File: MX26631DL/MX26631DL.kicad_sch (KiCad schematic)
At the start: 14 parts, among them U1 ESDBW5V0A1_C5173252, U2 MX26631DL

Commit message: Testboard is done, production files generated
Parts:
- removed C17: 100nF, Capacitor_SMD:C_0402_1005Metric, symbol Device:C
- removed U1: ESDBW5V0A1_C5173252, easyeda2kicad:X1-DFN1006-2_L1.0-W0.6-P0.65-BI, symbol TVS diode:ESDBW5V0A1_C5173252
- added U4: TPESD0402G15V, Diode_SMD:D_0402_1005Metric, symbol TVS diode:ESDBW5V0A1_C5173252
- C16: value 100nF -> 10uF; LCSC Part C1525 -> C315248
- R10: value 11kR -> 6.2kR; LCSC Part C2909313 -> C25915
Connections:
- net +5V_unprot: now also U4.1 (K)
- net GND: now also U4.2 (A)
- no-connect marks 11 -> 12
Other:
- note added: "For testing overvoltage and overcurrent capability. Overvoltage Threshold = 5.929v Overcurrent Threshold = 5.49A (8.235A in short bursts) Testing Over-voltage Protection V = 12V Testing Over-current Protection V = 5V - When testing overvoltage, a maximum of 12V to prevent LED burnout"
- note removed: "For testing overvoltage and overcurrent capability. Overvoltage = 6v Overcurrent = 3.26A(5A in short bursts) - When testing overvoltage, a maximum of 12V to prevent LED burnout"
- moved on the sheet: D1, R1

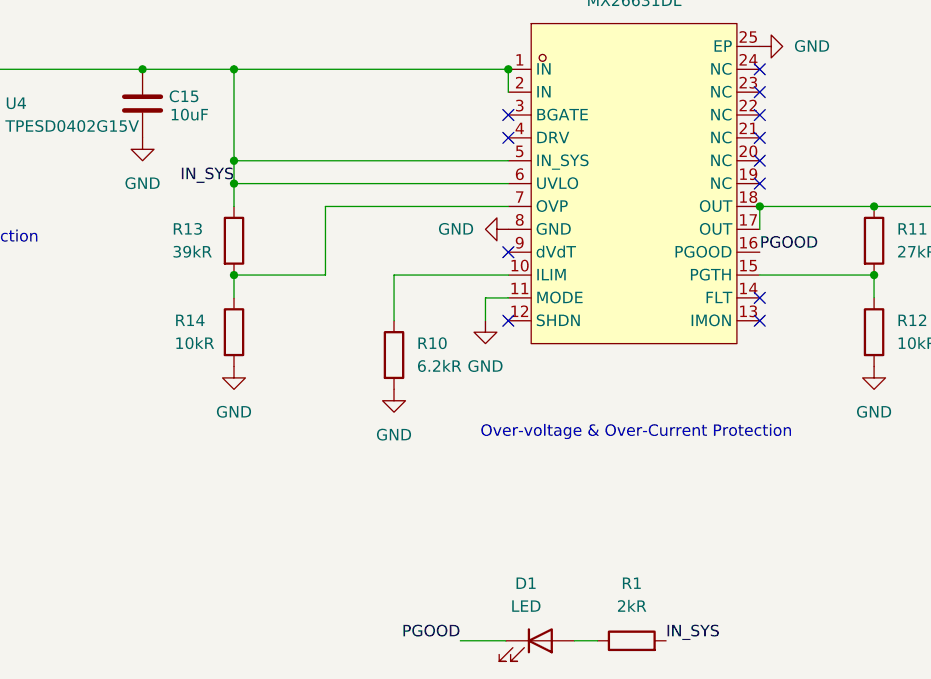
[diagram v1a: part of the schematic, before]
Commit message: Added dVdT capacitor to reduce current inrush. Production files generated
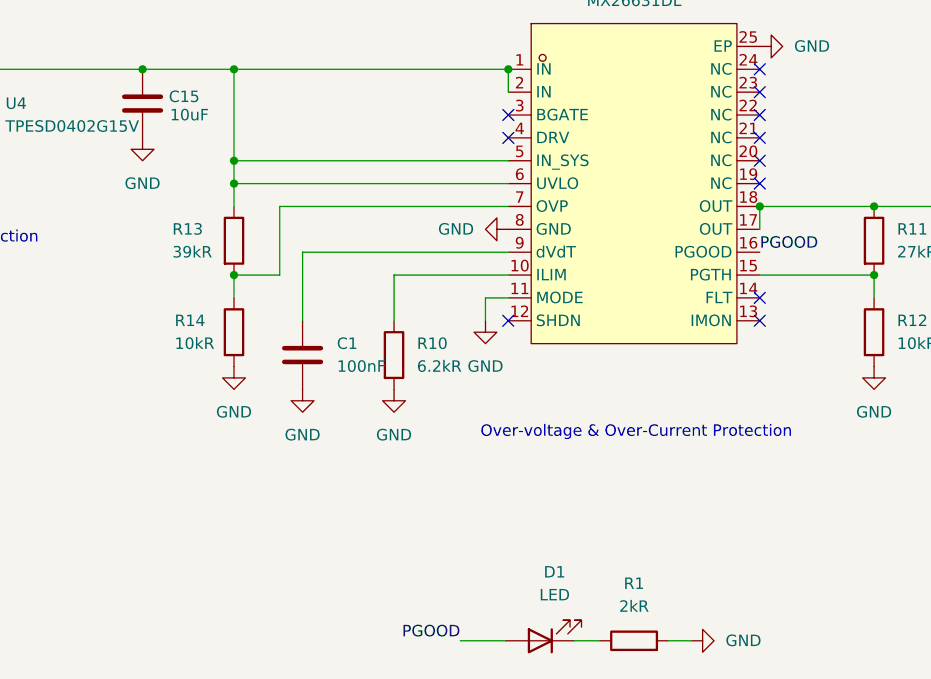
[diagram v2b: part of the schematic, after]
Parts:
- added C1: 100nF, Capacitor_SMD:C_0201_0603Metric, symbol Device:C
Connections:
- net +5V_unprot: no longer R1.2
- net GND: now also R1.2, C1.2
- net PGOOD: now also D1.2 (A); no longer D1.1 (K)
- net at R1.1: now also D1.1 (K); no longer D1.2 (A)
- net at U2.9 (dVdT): now also C1.1
- no-connect marks 12 -> 11
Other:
- moved on the sheet: D1

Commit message: Need to verify circuit 1 more time
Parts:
- removed C15, C16: 10uF, Capacitor_SMD:C_0402_1005Metric, symbol Device:C
- removed H1: X6511WV-02H-C30D60, easyeda2kicad:HDR-TH_2P-P2.54-V-M, symbol 2-pin header:X6511WV-02H-C30D60
- removed R2: 2R, Package_TO_SOT_SMD:TO-263-2, symbol Device:R
- added C2: 100nF, Capacitor_SMD:C_0402_1005Metric_Pad0.74x0.62mm_HandSolder, symbol Device:C
- added C3: 10uF, Capacitor_SMD:C_0805_2012Metric_Pad1.18x1.45mm_HandSolder, symbol Device:C
- added R7: 10R, Resistor_SMD:R_0603_1608Metric_Pad0.98x0.95mm_HandSolder, symbol Device:R
- added U1, U2: ZX-PZ2.54-1-1PZZ, easyeda2kicad:HDR-TH_1P-P2.54-V-M, symbol Pin header:ZX-PZ2.54-1-1PZZ
- C1: value 100nF -> 10uF; footprint Capacitor_SMD:C_0201_0603Metric -> Capacitor_SMD:C_0805_2012Metric_Pad1.18x1.45mm_HandSolder; LCSC Part C76939 -> C95841
- R1: renamed from R13; footprint Resistor_SMD:R_0402_1005Metric -> Resistor_SMD:R_0402_1005Metric_Pad0.72x0.64mm_HandSolder
- R2: renamed from R14; footprint Resistor_SMD:R_0402_1005Metric -> Resistor_SMD:R_0402_1005Metric_Pad0.72x0.64mm_HandSolder
- R3: renamed from R10; value 6.2kR -> 20kR; footprint Resistor_SMD:R_0402_1005Metric -> Resistor_SMD:R_0603_1608Metric_Pad0.98x0.95mm_HandSolder; LCSC Part C25915 -> C2907011
- R5: renamed from R11; value 27kR -> 31.6kR; footprint Resistor_SMD:R_0402_1005Metric -> Resistor_SMD:R_0603_1608Metric; LCSC Part C138022 -> C2933196
- R6: renamed from R12; footprint Resistor_SMD:R_0402_1005Metric -> Resistor_SMD:R_0402_1005Metric_Pad0.72x0.64mm_HandSolder
- renumbered R1 to R4, U4 to U3, U2 to U4
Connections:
- net +5V_unprot: now also C1.1, R4.2, U1.1
- net GND: now also C2.1, C3.2, R7.2, U2.1; no longer R4.2
- net PGOOD: now also D1.1 (K); no longer D1.2 (A)
- net at R4.1: now also D1.2 (A); no longer D1.1 (K)
- net at R5.1, U4.17 (OUT), U4.18 (OUT): now also C3.1, R7.1
- net at U4.9 (dVdT): now also C2.2; no longer C1.1
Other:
- note added: "PGOOD Trigger Voltage = 5.03V LED on = Fault LED off = Good"
- note added: "Testing Protection Over-voltage threshold Min Typ Max 5.782V < 5.929V < 6.174V Recovery voltage = 5.537V Testing Over-current Protection Min Typ Max 1.8A < 2.05A < 2.22A"
- note removed: "For testing overvoltage and overcurrent capability. Overvoltage Threshold = 5.929v Overcurrent Threshold = 5.49A (8.235A in short bursts) Testing Over-voltage Protection V = 12V Testing Over-current Protection V = 5V - When testing overvoltage, a maximum of 12V to prevent LED burnout"
- moved on the sheet: D1, R5, R6

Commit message: Time to test
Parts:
- R1: value 39kR -> 37.4kR; LCSC Part C2930006 -> C185422
- R5: value 31.6kR -> 29.4kR; LCSC Part C2933196 -> C2930086
- R7: footprint Resistor_SMD:R_0603_1608Metric_Pad0.98x0.95mm_HandSolder -> Resistor_SMD:R_2512_6332Metric_Pad1.40x3.35mm_HandSolder; LCSC Part C109318 -> C2075790
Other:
- note added: "Testing Protection Over-voltage threshold Min Typ Max 5.593V < 5.735V < 5.972V Recovery voltage = <5.356V Testing Over-current Protection Min Typ Max 1.8A < 2.05A < 2.22A"
- note removed: "Testing Protection Over-voltage threshold Min Typ Max 5.782V < 5.929V < 6.174V Recovery voltage = 5.537V Testing Over-current Protection Min Typ Max 1.8A < 2.05A < 2.22A"
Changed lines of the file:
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@@
 		)
 	)
-	(text "Testing Protection\n\nOver-voltage threshold\n\n  Min      Typ     Max\n5.782V < 5.929V < 6.174V\nRecovery voltage = 5.537V\n\nTesting Over-current Protection\n\n Min    Typ     Max\n1.8A < 2.05A < 2.22A\n\n"
+	(text "Testing Protection\n\nOver-voltage threshold\n\n  Min      Typ     Max\n5.593V < 5.735V < 5.972V\nRecovery voltage = <5.356V\n\nTesting Over-current Protection\n\n Min    Typ     Max\n1.8A < 2.05A < 2.22A\n\n"
 		(exclude_from_sim no)
 		(at 13.716 27.686 0)
@@
 		(dnp no)
 		(property "Reference" "R1"
-			(at 97.282 88.9 0)
+			(at 96.012 88.9 0)
 			(effects
 				(font
@@
 			)
 		)
-		(property "Value" "39kR"
-			(at 97.282 91.44 0)
+		(property "Value" "37.4kR"
+			(at 96.012 91.44 0)
 			(effects
 				(font
@@
 			)
 		)
-		(property "LCSC Part" "C2930006"
+		(property "LCSC Part" "C185422"
 			(at 104.14 90.17 0)
 			(effects
@@
 			)
 		)
-		(property "Footprint" "Resistor_SMD:R_0603_1608Metric_Pad0.98x0.95mm_HandSolder"
+		(property "Footprint" "Resistor_SMD:R_2512_6332Metric_Pad1.40x3.35mm_HandSolder"
 			(at 209.804 88.138 90)
 			(effects
@@
 			)
 		)
-		(property "LCSC Part" "C109318"
+		(property "LCSC Part" "C2075790"
 			(at 209.804 86.36 0)
 			(effects
@@
 			)
 		)
-		(property "Value" "31.6kR"
+		(property "Value" "29.4kR"
 			(at 183.134 91.4399 0)
 			(effects
@@
 			)
 		)
-		(property "LCSC Part" "C2933196"
+		(property "LCSC Part" "C2930086"
 			(at 180.594 90.17 0)
 			(effects
